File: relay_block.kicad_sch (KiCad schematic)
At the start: 49 parts, among them J4 Screw_Terminal_01x02, J5 Screw_Terminal_01x10, J6 Screw_Terminal_01x10, U10 TLP222A, U11 TLP222A, U12 TLP222A, U13 TLP222A, U14 TLP222A, U15 TLP222A, U16 TLP222A, U17 TLP222A, U18 TLP222A, U19 TLP222A, U20 TLP222A, U21 TLP222A, U22 TLP222A, U23 TLP222A, U24 TLP222A, U25 TLP222A, U4 TLP222A, U5 TLP222A, U6 TLP222A, U7 TLP222A, U8 TLP222A, U9 TLP222A

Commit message: Updated documentation
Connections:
- net In_HIGH renamed Out_HIGH
- net In_LOW renamed Out_LOW
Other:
- note added: "OUT A in the manual"
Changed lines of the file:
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@@
     (effects (font (size 1.27 1.27)) (justify left bottom))
   )
-  (label "In_HIGH" (at 130.81 124.46 90)
+  (text "OUT A in the manual" (at 53.34 25.4 0)
     (effects (font (size 1.27 1.27)) (justify left bottom))
   )
-  (label "In_LOW" (at 219.71 124.46 90)
+  (label "Out_HIGH" (at 130.81 124.46 90)
     (effects (font (size 1.27 1.27)) (justify left bottom))
   )
-  (label "In_HIGH" (at 237.49 124.46 90)
+  (label "Out_LOW" (at 219.71 124.46 90)
     (effects (font (size 1.27 1.27)) (justify left bottom))
   )
-  (label "In_HIGH" (at 236.22 48.26 90)
+  (label "Out_HIGH" (at 237.49 124.46 90)
     (effects (font (size 1.27 1.27)) (justify left bottom))
   )
-  (label "In_LOW" (at 147.32 48.26 90)
+  (label "Out_HIGH" (at 236.22 48.26 90)
     (effects (font (size 1.27 1.27)) (justify left bottom))
   )
-  (label "In_LOW" (at 62.23 48.26 90)
+  (label "Out_LOW" (at 147.32 48.26 90)
     (effects (font (size 1.27 1.27)) (justify left bottom))
   )
-  (label "In_HIGH" (at 200.66 48.26 90)
+  (label "Out_LOW" (at 62.23 48.26 90)
     (effects (font (size 1.27 1.27)) (justify left bottom))
   )
-  (label "In_HIGH" (at 166.37 124.46 90)
+  (label "Out_HIGH" (at 200.66 48.26 90)
     (effects (font (size 1.27 1.27)) (justify left bottom))
   )
-  (label "In_HIGH" (at 44.45 48.26 90)
+  (label "Out_HIGH" (at 166.37 124.46 90)
     (effects (font (size 1.27 1.27)) (justify left bottom))
   )
-  (label "In_LOW" (at 218.44 48.26 90)
+  (label "Out_HIGH" (at 44.45 48.26 90)
     (effects (font (size 1.27 1.27)) (justify left bottom))
   )
-  (label "In_HIGH" (at 129.54 48.26 90)
+  (label "Out_LOW" (at 218.44 48.26 90)
     (effects (font (size 1.27 1.27)) (justify left bottom))
   )
-  (label "In_HIGH" (at 43.18 24.13 0)
+  (label "Out_HIGH" (at 129.54 48.26 90)
     (effects (font (size 1.27 1.27)) (justify left bottom))
   )
-  (label "In_HIGH" (at 201.93 124.46 90)
+  (label "Out_HIGH" (at 43.18 24.13 0)
     (effects (font (size 1.27 1.27)) (justify left bottom))
   )
-  (label "In_LOW" (at 184.15 124.46 90)
+  (label "Out_HIGH" (at 201.93 124.46 90)
     (effects (font (size 1.27 1.27)) (justify left bottom))
   )
-  (label "In_LOW" (at 113.03 124.46 90)
+  (label "Out_LOW" (at 184.15 124.46 90)
     (effects (font (size 1.27 1.27)) (justify left bottom))
   )
-  (label "In_LOW" (at 255.27 124.46 90)
+  (label "Out_LOW" (at 113.03 124.46 90)
     (effects (font (size 1.27 1.27)) (justify left bottom))
   )
-  (label "In_LOW" (at 182.88 48.26 90)
+  (label "Out_LOW" (at 255.27 124.46 90)
     (effects (font (size 1.27 1.27)) (justify left bottom))
   )
-  (label "In_LOW" (at 254 48.26 90)
+  (label "Out_LOW" (at 182.88 48.26 90)
     (effects (font (size 1.27 1.27)) (justify left bottom))
   )
-  (label "In_LOW" (at 43.18 26.67 0)
+  (label "Out_LOW" (at 254 48.26 90)
     (effects (font (size 1.27 1.27)) (justify left bottom))
   )
-  (label "In_HIGH" (at 93.98 48.26 90)
+  (label "Out_LOW" (at 43.18 26.67 0)
     (effects (font (size 1.27 1.27)) (justify left bottom))
   )
-  (label "In_HIGH" (at 95.25 124.46 90)
+  (label "Out_HIGH" (at 93.98 48.26 90)
     (effects (font (size 1.27 1.27)) (justify left bottom))
   )
-  (label "In_HIGH" (at 165.1 48.26 90)
+  (label "Out_HIGH" (at 95.25 124.46 90)
     (effects (font (size 1.27 1.27)) (justify left bottom))
   )
-  (label "In_LOW" (at 148.59 124.46 90)
+  (label "Out_HIGH" (at 165.1 48.26 90)
     (effects (font (size 1.27 1.27)) (justify left bottom))
   )
-  (label "In_LOW" (at 111.76 48.26 90)
+  (label "Out_LOW" (at 148.59 124.46 90)
     (effects (font (size 1.27 1.27)) (justify left bottom))
   )
+  (label "Out_LOW" (at 111.76 48.26 90)
+    (effects (font (size 1.27 1.27)) (justify left bottom))
+  )

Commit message: Updated BOM
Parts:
- U10, U11, U12, U13, U14, U16, U17, U18, U19, U20, U21, U22, U23, U24, U25, U4, U5, U6, U7, U8, U9: value TLP222A -> TLP3558A; MFN (none) -> Toshiba; PN (none) -> TLP3558A(F
- U15: value TLP222A -> TLP3558A

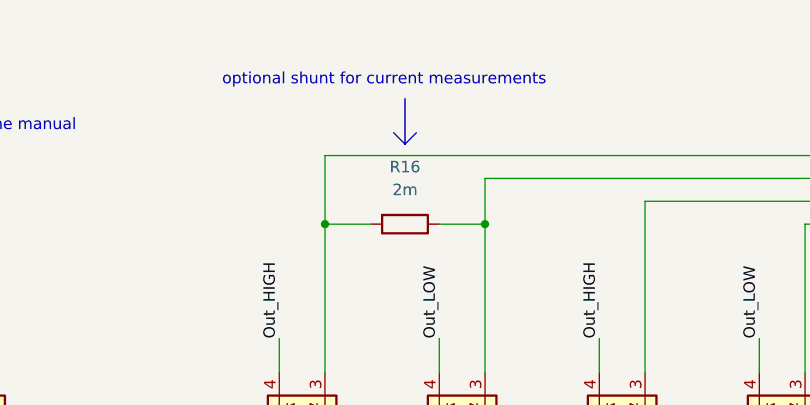
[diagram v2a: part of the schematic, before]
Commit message: Updated to KiCad 8 (#1)
- Updated libraries
- Updated BOM, replaced obsolete parts
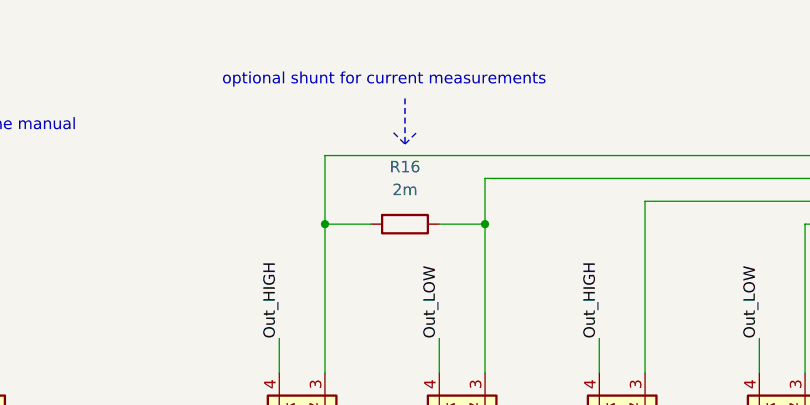
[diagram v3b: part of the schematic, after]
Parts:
- J4, J5, J6: RoHS (none) -> By exemption; Temperature (none) -> Tstorage = –40 °C to 105 °C
- R12, R13, R14, R15, R18, R19, R20, R21, R22, R23, R24, R25, R26, R27, R28, R29, R30, R31, R32, R33, R34, R35: RoHS (none) -> By exemption; Temperature (none) -> Tstorage = –55 °C to 155 °C
- R16, R17: RoHS (none) -> Yes; Temperature (none) -> Tstorage = –55 °C to 170 °C
- U10, U11, U12, U13, U14, U15, U16, U17, U18, U19, U20, U21, U22, U23, U24, U25, U4, U5, U6, U7, U8, U9: RoHS (none) -> Yes; Temperature (none) -> Tstorage = –20 °C to 85 °C
